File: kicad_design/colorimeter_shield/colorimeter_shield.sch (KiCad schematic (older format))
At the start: 9 parts, among them K1 CONN_3, P1 CONN_4, P2 CONN_5X2, P3 CONN_2, P4 CONN_2, SW1 SW_PUSH

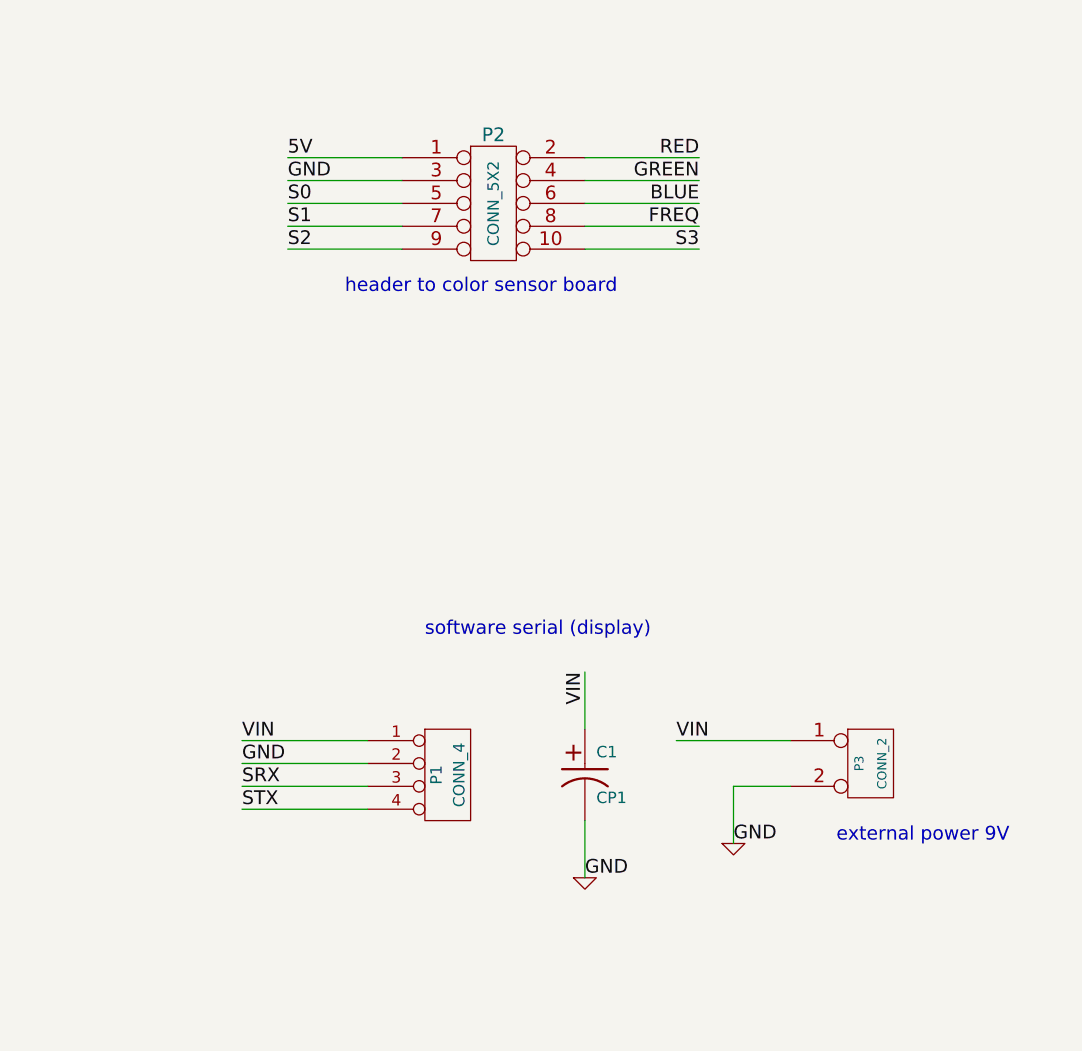
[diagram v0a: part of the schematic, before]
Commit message: Finished designing Arduino shield PCB for the colorimeter.
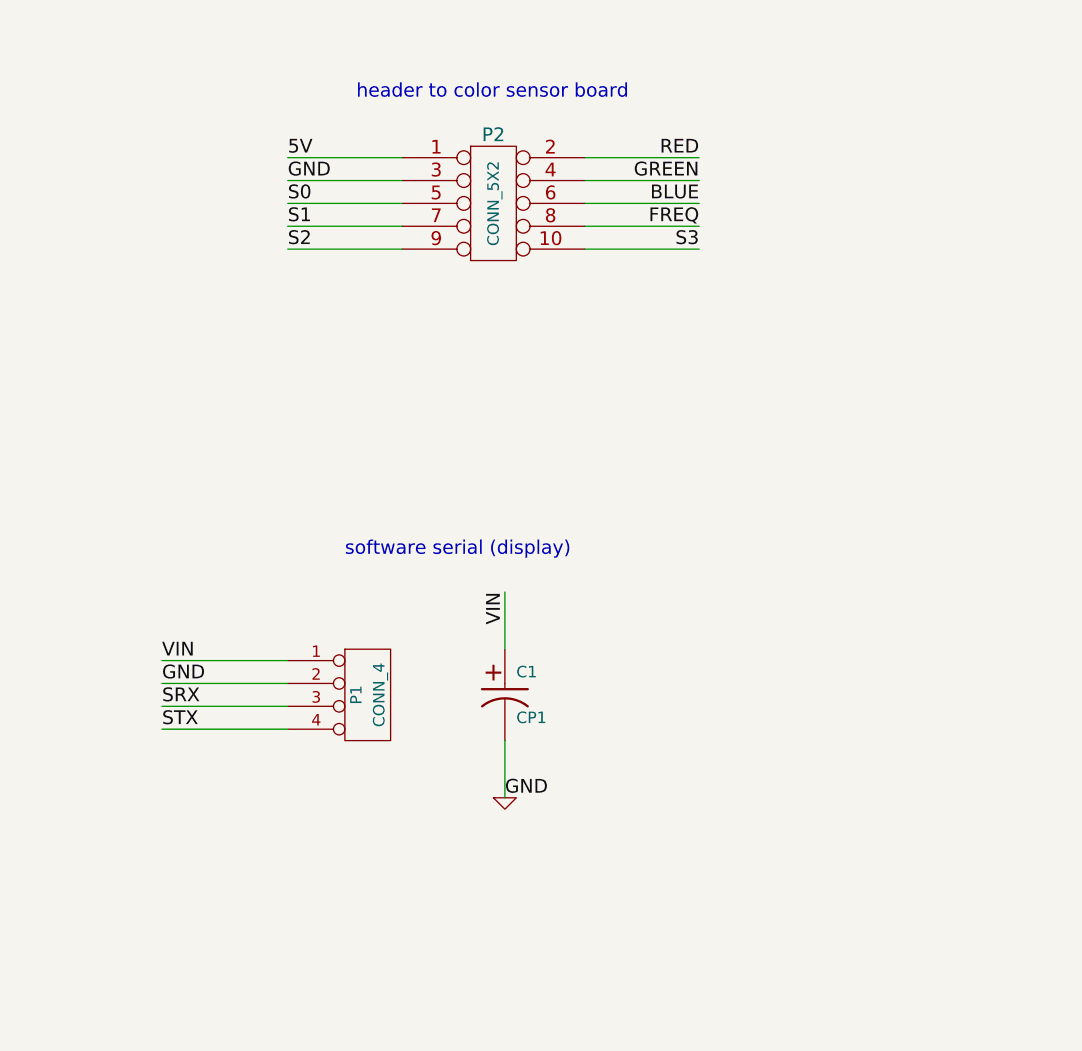
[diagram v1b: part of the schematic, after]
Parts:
- removed P3: CONN_2, symbol CONN_2
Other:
- note removed: "external power 9V"
- moved on the sheet: C1, P1
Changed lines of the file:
@@
-EESchema Schematic File Version 2  date Wed 04 Jan 2012 04:01:56 PM PST
+EESchema Schematic File Version 2  date Mon 09 Jan 2012 06:30:10 PM PST
 LIBS:power
 LIBS:device
@@
 Sheet 1 1
 Title ""
-Date "4 jan 2012"
+Date "10 jan 2012"
 Rev ""
 Comp ""
@@
 	5050 1300 5550 1300
 Wire Wire Line
-	8550 4350 8550 4600
-Wire Wire Line
-	9200 4450 9200 4200
-Wire Wire Line
-	9200 4200 9450 4200
+	8200 4000 8200 4250
 Wire Wire Line
 	5050 2000 5550 2000
@@
 	3150 2000 2650 2000
 Wire Wire Line
-	7600 4200 7050 4200
-Wire Wire Line
-	7600 4000 7050 4000
+	7250 3850 6700 3850
+Wire Wire Line
+	7250 3650 6700 3650
 Wire Wire Line
 	8550 1750 9050 1750
@@
 	8550 1850 9050 1850
 Wire Wire Line
-	7600 4100 7050 4100
-Wire Wire Line
-	7600 4300 7050 4300
+	7250 3750 6700 3750
+Wire Wire Line
+	7250 3950 6700 3950
 Wire Wire Line
 	5050 2100 5550 2100
 Wire Wire Line
-	9450 4000 8950 4000
-Wire Wire Line
-	8550 3950 8550 3700
+	8200 3600 8200 3350
 Wire Wire Line
 	5050 1400 5550 1400
@@
 Wire Wire Line
 	2050 1100 2050 1400
-Text Notes 9650 4450 0    60   ~ 0
-external power 9V
 Text Label 2050 1400 0    60   ~ 0
 5V
@@
 Text Label 5550 1400 2    60   ~ 0
 SRX
-Text Label 8550 3700 3    60   ~ 0
+Text Label 8200 3350 3    60   ~ 0
 VIN
-Text Label 8550 4600 0    60   ~ 0
+Text Label 8200 4250 0    60   ~ 0
 GND
 $Comp
 L GND #PWR06
 U 1 1 4F04AA6D
-P 8550 4600
-F 0 "#PWR06" H 8550 4600 30  0001 C CNN
-F 1 "GND" H 8550 4530 30  0001 C CNN
-	1    8550 4600
+P 8200 4250
+F 0 "#PWR06" H 8200 4250 30  0001 C CNN
+F 1 "GND" H 8200 4180 30  0001 C CNN
+	1    8200 4250
 	1    0    0    -1
 $EndComp
@@
 L CP1 C1
 U 1 1 4F04AA4F
-P 8550 4150
-F 0 "C1" H 8600 4250 50  0000 L CNN
-F 1 "CP1" H 8600 4050 50  0000 L CNN
-	1    8550 4150
-	1    0    0    -1
-$EndComp
-Text Label 8950 4000 0    60   ~ 0
-VIN
-Text Label 9200 4450 0    60   ~ 0
-GND
-$Comp
-L GND #PWR07
-U 1 1 4F04AA18
-P 9200 4450
-F 0 "#PWR07" H 9200 4450 30  0001 C CNN
-F 1 "GND" H 9200 4380 30  0001 C CNN
-	1    9200 4450
-	1    0    0    -1
-$EndComp
-$Comp
-L CONN_2 P3
-U 1 1 4F04A9DF
-P 9800 4100
-F 0 "P3" V 9750 4100 40  0000 C CNN
-F 1 "CONN_2" V 9850 4100 40  0000 C CNN
-	1    9800 4100
+P 8200 3800
+F 0 "C1" H 8250 3900 50  0000 L CNN
+F 1 "CP1" H 8250 3700 50  0000 L CNN
+	1    8200 3800
 	1    0    0    -1
 $EndComp
@@
 Text Label 2650 2000 0    60   ~ 0
 VIN
-Text Notes 7500 2050 0    60   ~ 0
+Text Notes 7550 1200 0    60   ~ 0
 header to color sensor board
-Text Notes 7850 3550 0    60   ~ 0
+Text Notes 7500 3200 0    60   ~ 0
 software serial (display)
-Text Label 7050 4300 0    60   ~ 0
+Text Label 6700 3950 0    60   ~ 0
 STX
-Text Label 7050 4200 0    60   ~ 0
+Text Label 6700 3850 0    60   ~ 0
 SRX
-Text Label 7050 4100 0    60   ~ 0
-GND
-Text Label 7050 4000 0    60   ~ 0
+Text Label 6700 3750 0    60   ~ 0
+GND
+Text Label 6700 3650 0    60   ~ 0
 VIN
 $Comp
 L CONN_4 P1
 U 1 1 4F04A60F
-P 7950 4150
-F 0 "P1" V 7900 4150 50  0000 C CNN
-F 1 "CONN_4" V 8000 4150 50  0000 C CNN
-	1    7950 4150
-	1    0    0    -1
-$EndComp
+P 7600 3800
+F 0 "P1" V 7550 3800 50  0000 C CNN
+F 1 "CONN_4" V 7650 3800 50  0000 C CNN
+	1    7600 3800
+	1    0    0    -1
+$EndComp

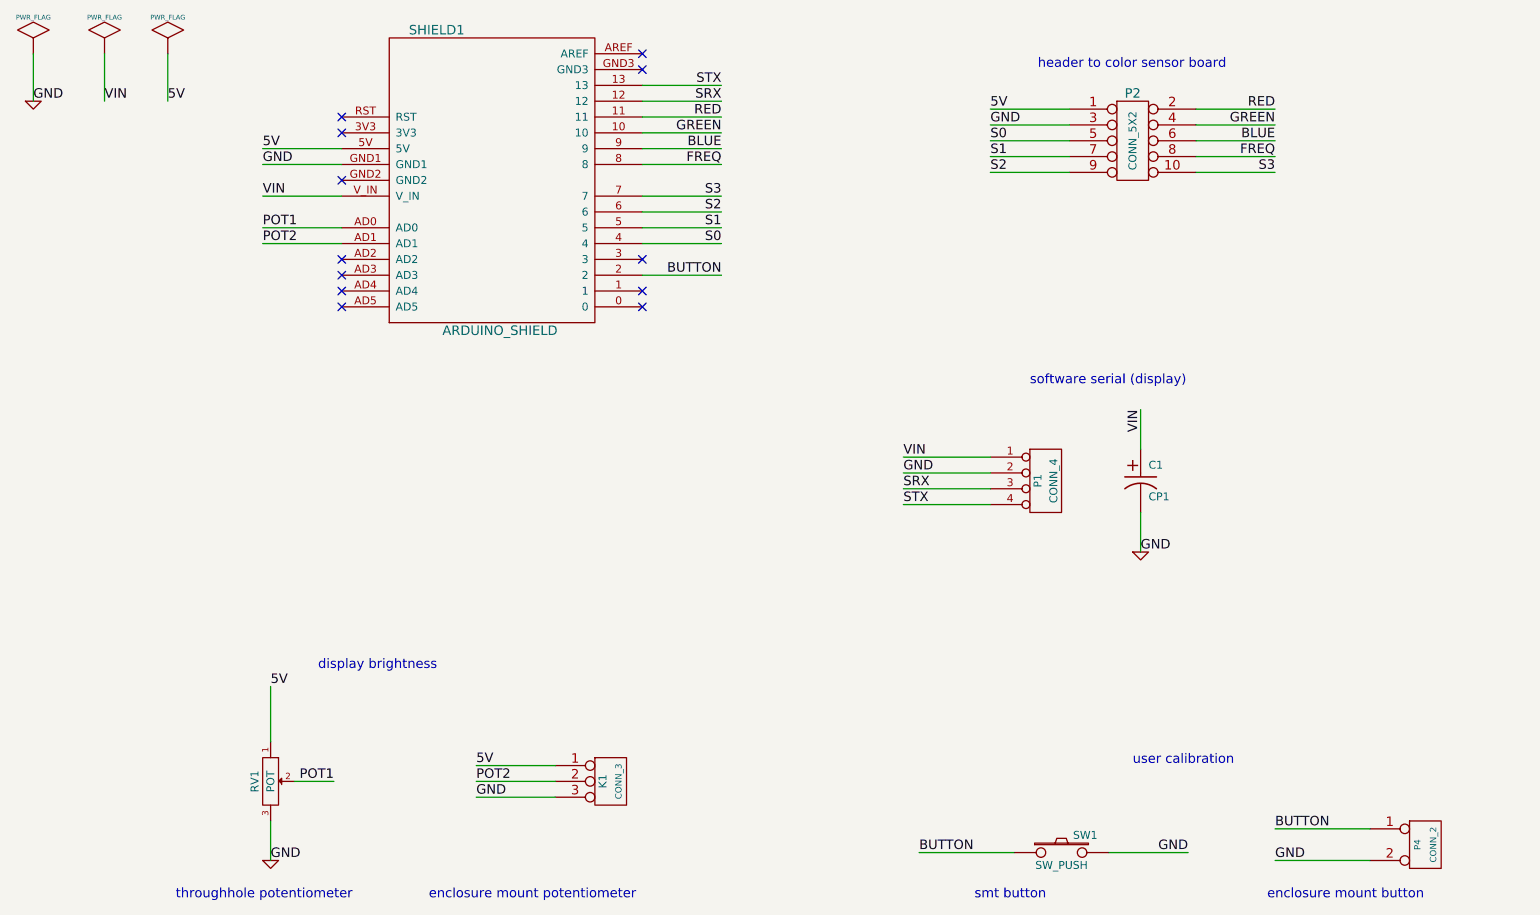
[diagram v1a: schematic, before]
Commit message: Version 2 of the colorimeter. Removed alot of the components that are not necessary to make a very basic breakout board.
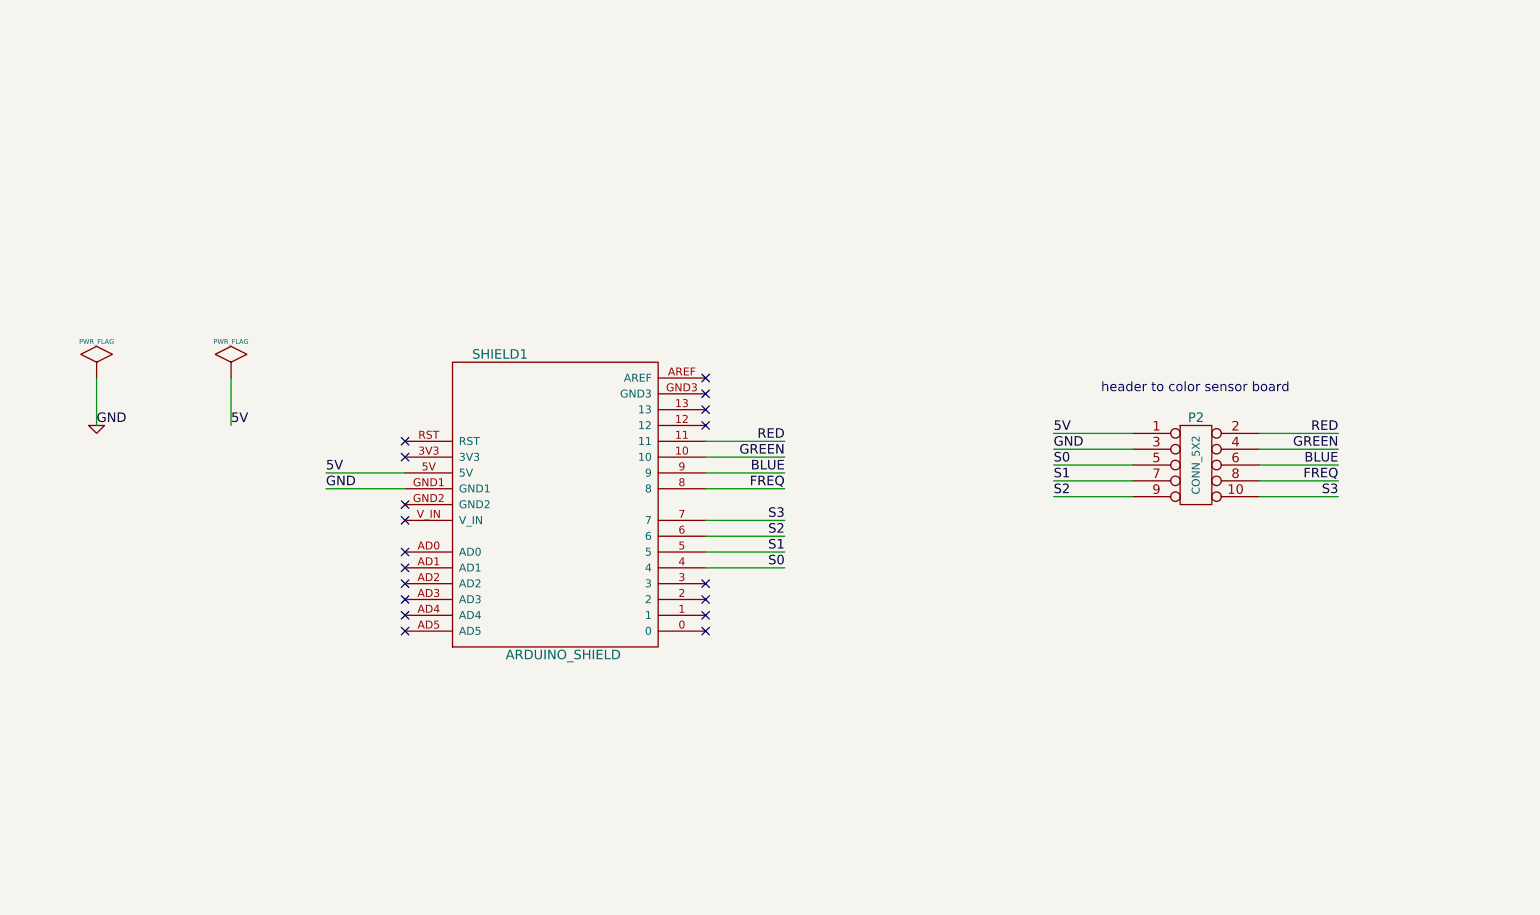
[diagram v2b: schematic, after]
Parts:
- removed C1: CP1, symbol CP1
- removed K1: CONN_3, symbol CONN_3
- removed P1: CONN_4, symbol CONN_4
- removed P4: CONN_2, symbol CONN_2
- removed RV1: POT, symbol POT
- removed SW1: SW_PUSH, symbol SW_PUSH
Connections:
- net BUTTON: no longer names the net of SHIELD1.2
- net POT1: no longer names the net of SHIELD1.AD0
- net POT2: no longer names the net of SHIELD1.AD1
- net SRX: no longer names the net of SHIELD1.12
- net STX: no longer names the net of SHIELD1.13
- net VIN: no longer names the net of SHIELD1.V_IN
- no-connect marks 12 -> 18
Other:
- note removed: "display brightness"
- note removed: "enclosure mount button"
- note removed: "enclosure mount potentiometer"
- note removed: "smt button"
- note removed: "software serial (display)"
- note removed: "throughhole potentiometer"
- note removed: "user calibration"
- moved on the sheet: P2, SHIELD1

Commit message: version 2p0 gerber files for sensor, led and shield boards.
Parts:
- renumbered P2 to P1
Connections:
- net GND: now also SHIELD1.GND3
- no-connect marks 18 -> 17
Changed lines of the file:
@@
-EESchema Schematic File Version 2  date Fri 10 Feb 2012 11:31:22 AM PST
+EESchema Schematic File Version 2  date Fri 10 Feb 2012 12:57:47 PM PST
 LIBS:power
 LIBS:device
@@
 Comment4 ""
 $EndDescr
+Text Label 5950 3250 2    60   ~ 0
+GND
+Wire Wire Line
+	5450 3250 5950 3250
+Wire Wire Line
+	2450 3150 2450 3450
+Wire Wire Line
+	1600 3150 1600 3450
+Wire Wire Line
+	5450 4150 5950 4150
+Wire Wire Line
+	8950 3900 9450 3900
+Wire Wire Line
+	8950 3700 9450 3700
+Wire Wire Line
+	8950 3500 9450 3500
+Wire Wire Line
+	8150 3800 7650 3800
+Wire Wire Line
+	8150 3600 7650 3600
+Wire Wire Line
+	5450 4350 5950 4350
+Wire Wire Line
+	5450 3650 5950 3650
+Wire Wire Line
+	5450 3850 5950 3850
+Wire Wire Line
+	3550 3750 3050 3750
+Wire Wire Line
+	3550 3850 3050 3850
+Wire Wire Line
+	5450 3750 5950 3750
+Wire Wire Line
+	5450 3550 5950 3550
+Wire Wire Line
+	5450 4250 5950 4250
+Wire Wire Line
+	8150 3500 7650 3500
+Wire Wire Line
+	8150 3700 7650 3700
+Wire Wire Line
+	8150 3900 7650 3900
+Wire Wire Line
+	8950 3600 9450 3600
+Wire Wire Line
+	8950 3800 9450 3800
+Wire Wire Line
+	5450 4050 5950 4050
 NoConn ~ 5450 4550
 NoConn ~ 3550 4350
@@
 NoConn ~ 5450 3450
 NoConn ~ 5450 3350
-Wire Wire Line
-	5450 4050 5950 4050
-Wire Wire Line
-	8950 3800 9450 3800
-Wire Wire Line
-	8950 3600 9450 3600
-Wire Wire Line
-	8150 3900 7650 3900
-Wire Wire Line
-	8150 3700 7650 3700
-Wire Wire Line
-	8150 3500 7650 3500
-Wire Wire Line
-	5450 4250 5950 4250
-Wire Wire Line
-	5450 3550 5950 3550
-Wire Wire Line
-	5450 3750 5950 3750
-Wire Wire Line
-	3550 3850 3050 3850
-Wire Wire Line
-	3550 3750 3050 3750
-Wire Wire Line
-	5450 3850 5950 3850
-Wire Wire Line
-	5450 3650 5950 3650
-Wire Wire Line
-	5450 4350 5950 4350
-Wire Wire Line
-	8150 3600 7650 3600
-Wire Wire Line
-	8150 3800 7650 3800
-Wire Wire Line
-	8950 3500 9450 3500
-Wire Wire Line
-	8950 3700 9450 3700
-Wire Wire Line
-	8950 3900 9450 3900
-Wire Wire Line
-	5450 4150 5950 4150
-Wire Wire Line
-	1600 3150 1600 3450
-Wire Wire Line
-	2450 3150 2450 3450
 Text Label 2450 3450 0    60   ~ 0
 5V
@@
 NoConn ~ 5450 4750
 NoConn ~ 5450 4650
-NoConn ~ 5450 3250
 NoConn ~ 5450 3150
 Text Label 3050 3850 0    60   ~ 0
@@
 $EndComp
 $Comp
-L CONN_5X2 P2
+L CONN_5X2 P1
 U 1 1 4F03AC98
 P 8550 3700
-F 0 "P2" H 8550 4000 60  0000 C CNN
+F 0 "P1" H 8550 4000 60  0000 C CNN
 F 1 "CONN_5X2" V 8550 3700 50  0000 C CNN
 	1    8550 3700
